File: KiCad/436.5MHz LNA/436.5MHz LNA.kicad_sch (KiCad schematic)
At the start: 15 parts, among them J1 Conn_Coaxial, J2 Conn_Coaxial, J3 +9V, Q1 J310

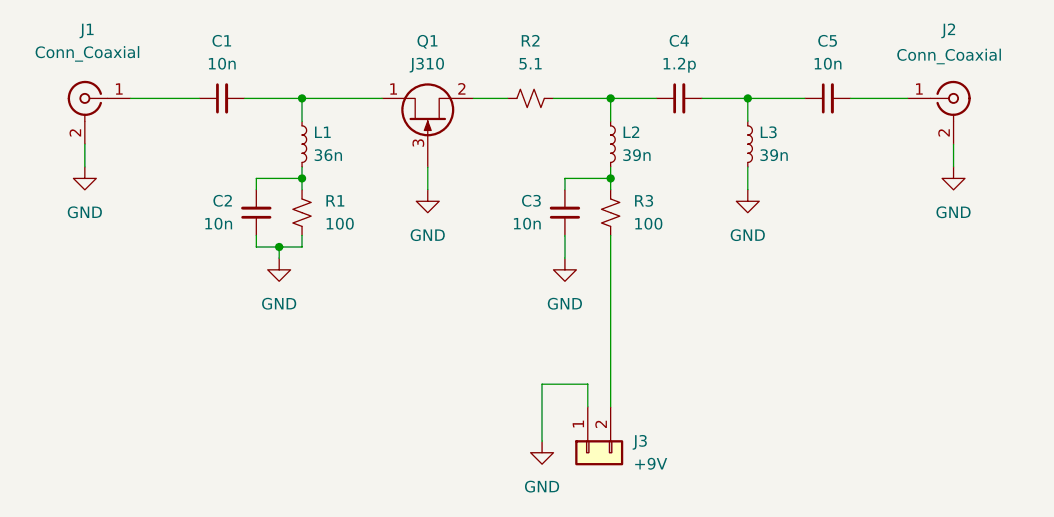
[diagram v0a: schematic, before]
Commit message: added BOM
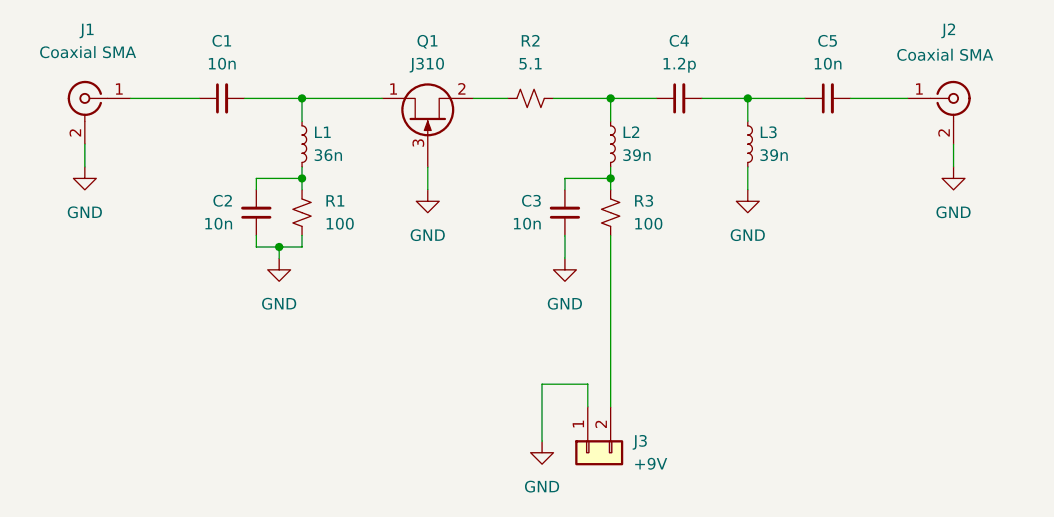
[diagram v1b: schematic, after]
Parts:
- J1, J2: value Conn_Coaxial -> Coaxial SMA
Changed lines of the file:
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@@
   (title_block
     (title "436.5MHz LNA")
+    (rev "1.0")
     (company "KK7DLH")
   )
@@
     (in_bom yes) (on_board yes) (fields_autoplaced)
     (property "Reference" "J1" (id 0) (at 94.2974 81.28 0))
-    (property "Value" "Conn_Coaxial" (id 1) (at 94.2974 83.82 0))
+    (property "Value" "Coaxial SMA" (id 1) (at 94.2974 83.82 0))
     (property "Footprint" "Connector_Coaxial:SMA_Amphenol_132289_EdgeMount" (id 2) (at 93.98 88.9 0)
       (effects (font (size 1.27 1.27)) hide)
@@
       (effects (font (size 1.27 1.27)) (justify left))
     )
-    (property "Value" "Conn_Coaxial" (id 1) (at 184.15 84.1131 0)
+    (property "Value" "Coaxial SMA" (id 1) (at 184.15 84.1131 0)
       (effects (font (size 1.27 1.27)) (justify left))
     )
@@
     )
     (path "/e04409c2-b3ba-460e-bddc-62e0044901c2"
-      (reference "J1") (unit 1) (value "Conn_Coaxial") (footprint "Connector_Coaxial:SMA_Amphenol_132289_EdgeMount")
+      (reference "J1") (unit 1) (value "Coaxial SMA") (footprint "Connector_Coaxial:SMA_Amphenol_132289_EdgeMount")
     )
     (path "/f0ff0792-4d97-4881-9b9c-759645b25c42"
-      (reference "J2") (unit 1) (value "Conn_Coaxial") (footprint "Connector_Coaxial:SMA_Amphenol_132289_EdgeMount")
+      (reference "J2") (unit 1) (value "Coaxial SMA") (footprint "Connector_Coaxial:SMA_Amphenol_132289_EdgeMount")
     )
     (path "/45c0d4b2-152f-4522-afdb-d5657a7cd4e7"

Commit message: updated bom to purchase inductors from coilcraft and to remove most parts with terifs
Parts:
- C1, C2, C3, C5: DPN 478-10055-2-ND -> 1276-1091-2-ND; MFN KYOCERA AVX -> Samsung Electro-Mechanics; MPN 06035C103KAT4A -> CL10C102JB8NNNC
- C4: DPN 311-3825-2-ND -> 311-3825-1-ND‎; MPN CC0603BRNPO9BN1R2 -> CC0603BRNPO9BN1R2‎
- J1, J2: DPN 314-1702-ND -> 314-1702-ND‎
- L1: DPN 2457-0603DC-36NXJRW-ND -> 0603DC-36NXJRW; Dist DigiKey -> Coilcraft
- L2, L3: DPN 2457-0603DC-39NXJRW-ND -> 0603DC-39NXJRW; Dist DigiKey -> Coilcraft
- Q1: DPN MMBFJ310LT3GOSTR-ND -> MMBFJ310LT3GOSCT-ND‎
- R1, R3: DPN 541-CRCW0603100RFKEBCTR-ND -> A129676TR-ND; MFN Vishay Dale -> TE Connectivity Passive Product; MPN CRCW0603100RFKEBC -> CRGCQ0603F100R
- R2: DPN YAG3372TR-ND -> YAG3372CT-ND‎
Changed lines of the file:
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@@
       (effects (font (size 1.27 1.27)) hide)
     )
-    (property "DPN" "478-10055-2-ND" (id 5) (at 109.22 88.9 0)
-      (effects (font (size 1.27 1.27)) hide)
-    )
-    (property "MFN" "KYOCERA AVX" (id 6) (at 109.22 88.9 0)
-      (effects (font (size 1.27 1.27)) hide)
-    )
-    (property "MPN" "06035C103KAT4A" (id 7) (at 109.22 88.9 0)
+    (property "DPN" "1276-1091-2-ND" (id 5) (at 109.22 88.9 0)
+      (effects (font (size 1.27 1.27)) hide)
+    )
+    (property "MFN" "Samsung Electro-Mechanics" (id 6) (at 109.22 88.9 0)
+      (effects (font (size 1.27 1.27)) hide)
+    )
+    (property "MPN" "CL10C102JB8NNNC" (id 7) (at 109.22 88.9 0)
       (effects (font (size 1.27 1.27)) hide)
     )
@@
       (effects (font (size 1.27 1.27)) hide)
     )
-    (property "DPN" "541-CRCW0603100RFKEBCTR-ND" (id 5) (at 118.11 101.6 0)
-      (effects (font (size 1.27 1.27)) hide)
-    )
-    (property "MFN" "Vishay Dale" (id 6) (at 118.11 101.6 0)
-      (effects (font (size 1.27 1.27)) hide)
-    )
-    (property "MPN" "CRCW0603100RFKEBC" (id 7) (at 118.11 101.6 0)
+    (property "DPN" "A129676TR-ND" (id 5) (at 118.11 101.6 0)
+      (effects (font (size 1.27 1.27)) hide)
+    )
+    (property "MFN" "TE Connectivity Passive Product" (id 6) (at 118.11 101.6 0)
+      (effects (font (size 1.27 1.27)) hide)
+    )
+    (property "MPN" "CRGCQ0603F100R" (id 7) (at 118.11 101.6 0)
       (effects (font (size 1.27 1.27)) hide)
     )
@@
       (effects (font (size 1.27 1.27)) hide)
     )
-    (property "Dist" "DigiKey" (id 6) (at 167.64 93.98 0)
-      (effects (font (size 1.27 1.27)) hide)
-    )
-    (property "DPN" "2457-0603DC-39NXJRW-ND" (id 7) (at 167.64 93.98 0)
+    (property "Dist" "Coilcraft" (id 6) (at 167.64 93.98 0)
+      (effects (font (size 1.27 1.27)) hide)
+    )
+    (property "DPN" "0603DC-39NXJRW" (id 7) (at 167.64 93.98 0)
       (effects (font (size 1.27 1.27)) hide)
     )
@@
       (effects (font (size 1.27 1.27)) hide)
     )
-    (property "DPN" "2457-0603DC-36NXJRW-ND" (id 4) (at 118.11 93.98 0)
-      (effects (font (size 1.27 1.27)) hide)
-    )
-    (property "Dist" "DigiKey" (id 5) (at 118.11 93.98 0)
+    (property "DPN" "0603DC-36NXJRW" (id 4) (at 118.11 93.98 0)
+      (effects (font (size 1.27 1.27)) hide)
+    )
+    (property "Dist" "Coilcraft" (id 5) (at 118.11 93.98 0)
       (effects (font (size 1.27 1.27)) hide)
     )
@@
       (effects (font (size 1.27 1.27)) hide)
     )
-    (property "DPN" "478-10055-2-ND" (id 5) (at 176.53 88.9 0)
-      (effects (font (size 1.27 1.27)) hide)
-    )
-    (property "MFN" "KYOCERA AVX" (id 6) (at 176.53 88.9 0)
-      (effects (font (size 1.27 1.27)) hide)
-    )
-    (property "MPN" "06035C103KAT4A" (id 7) (at 176.53 88.9 0)
+    (property "DPN" "1276-1091-2-ND" (id 5) (at 176.53 88.9 0)
+      (effects (font (size 1.27 1.27)) hide)
+    )
+    (property "MFN" "Samsung Electro-Mechanics" (id 6) (at 176.53 88.9 0)
+      (effects (font (size 1.27 1.27)) hide)
+    )
+    (property "MPN" "CL10C102JB8NNNC" (id 7) (at 176.53 88.9 0)
       (effects (font (size 1.27 1.27)) hide)
     )
@@
       (effects (font (size 1.27 1.27)) hide)
     )
-    (property "DPN" "541-CRCW0603100RFKEBCTR-ND" (id 5) (at 152.4 101.6 0)
-      (effects (font (size 1.27 1.27)) hide)
-    )
-    (property "MFN" "Vishay Dale" (id 6) (at 152.4 101.6 0)
-      (effects (font (size 1.27 1.27)) hide)
-    )
-    (property "MPN" "CRCW0603100RFKEBC" (id 7) (at 152.4 101.6 0)
+    (property "DPN" "A129676TR-ND" (id 5) (at 152.4 101.6 0)
+      (effects (font (size 1.27 1.27)) hide)
+    )
+    (property "MFN" "TE Connectivity Passive Product" (id 6) (at 152.4 101.6 0)
+      (effects (font (size 1.27 1.27)) hide)
+    )
+    (property "MPN" "CRGCQ0603F100R" (id 7) (at 152.4 101.6 0)
       (effects (font (size 1.27 1.27)) hide)
     )
@@
       (effects (font (size 1.27 1.27)) hide)
     )
-    (property "DPN" "478-10055-2-ND" (id 5) (at 147.32 101.6 0)
-      (effects (font (size 1.27 1.27)) hide)
-    )
-    (property "MFN" "KYOCERA AVX" (id 6) (at 147.32 101.6 0)
-      (effects (font (size 1.27 1.27)) hide)
-    )
-    (property "MPN" "06035C103KAT4A" (id 7) (at 147.32 101.6 0)
+    (property "DPN" "1276-1091-2-ND" (id 5) (at 147.32 101.6 0)
+      (effects (font (size 1.27 1.27)) hide)
+    )
+    (property "MFN" "Samsung Electro-Mechanics" (id 6) (at 147.32 101.6 0)
+      (effects (font (size 1.27 1.27)) hide)
+    )
+    (property "MPN" "CL10C102JB8NNNC" (id 7) (at 147.32 101.6 0)
       (effects (font (size 1.27 1.27)) hide)
     )
@@
       (effects (font (size 1.27 1.27)) hide)
     )
-    (property "DPN" "311-3825-2-ND" (id 5) (at 160.02 88.9 0)
+    (property "DPN" "311-3825-1-ND‎" (id 5) (at 160.02 88.9 0)
       (effects (font (size 1.27 1.27)) hide)
     )
@@
       (effects (font (size 1.27 1.27)) hide)
     )
-    (property "MPN" "CC0603BRNPO9BN1R2" (id 7) (at 160.02 88.9 0)
+    (property "MPN" "CC0603BRNPO9BN1R2‎ " (id 7) (at 160.02 88.9 0)
       (effects (font (size 1.27 1.27)) hide)
     )
@@
       (effects (font (size 1.27 1.27)) hide)
     )
-    (property "DPN" "314-1702-ND" (id 5) (at 93.98 88.9 0)
+    (property "DPN" "314-1702-ND‎" (id 5) (at 93.98 88.9 0)
       (effects (font (size 1.27 1.27)) hide)
     )
@@
       (effects (font (size 1.27 1.27)) hide)
     )
-    (property "DPN" "YAG3372TR-ND" (id 5) (at 143.51 88.9 0)
+    (property "DPN" "YAG3372CT-ND‎" (id 5) (at 143.51 88.9 0)
       (effects (font (size 1.27 1.27)) hide)
     )
@@
       (effects (font (size 1.27 1.27)) hide)
     )
-    (property "DPN" "478-10055-2-ND" (id 5) (at 113.03 101.6 0)
-      (effects (font (size 1.27 1.27)) hide)
-    )
-    (property "MFN" "KYOCERA AVX" (id 6) (at 113.03 101.6 0)
-      (effects (font (size 1.27 1.27)) hide)
-    )
-    (property "MPN" "06035C103KAT4A" (id 7) (at 113.03 101.6 0)
+    (property "DPN" "1276-1091-2-ND" (id 5) (at 113.03 101.6 0)
+      (effects (font (size 1.27 1.27)) hide)
+    )
+    (property "MFN" "Samsung Electro-Mechanics" (id 6) (at 113.03 101.6 0)
+      (effects (font (size 1.27 1.27)) hide)
+    )
+    (property "MPN" "CL10C102JB8NNNC" (id 7) (at 113.03 101.6 0)
       (effects (font (size 1.27 1.27)) hide)
     )
@@
       (effects (font (size 1.27 1.27)) hide)
     )
-    (property "DPN" "MMBFJ310LT3GOSTR-ND" (id 4) (at 132.08 91.44 0)
+    (property "DPN" "MMBFJ310LT3GOSCT-ND‎" (id 4) (at 132.08 91.44 0)
       (effects (font (size 1.27 1.27)) hide)
     )
@@
       (effects (font (size 1.27 1.27)) hide)
     )
-    (property "DPN" "314-1702-ND" (id 5) (at 190.5 88.9 0)
+    (property "DPN" "314-1702-ND‎" (id 5) (at 190.5 88.9 0)
       (effects (font (size 1.27 1.27)) hide)
     )
@@
       (effects (font (size 1.27 1.27)) hide)
     )
-    (property "DPN" "2457-0603DC-39NXJRW-ND" (id 4) (at 152.4 93.98 0)
-      (effects (font (size 1.27 1.27)) hide)
-    )
-    (property "Dist" "DigiKey" (id 5) (at 152.4 93.98 0)
-      (effects (font (size 1.27 1.27)) hide)
-    )
+    (property "DPN" "0603DC-39NXJRW" (id 4) (at 152.4 93.98 0)
+      (effects (font (size 1.27 1.27)) hide)
+    )
+    (property "Dist" "Coilcraft" (id 5) (at 152.4 93.98 0)
+      (effects (font (size 1.27 1.27)) hide)
+    )

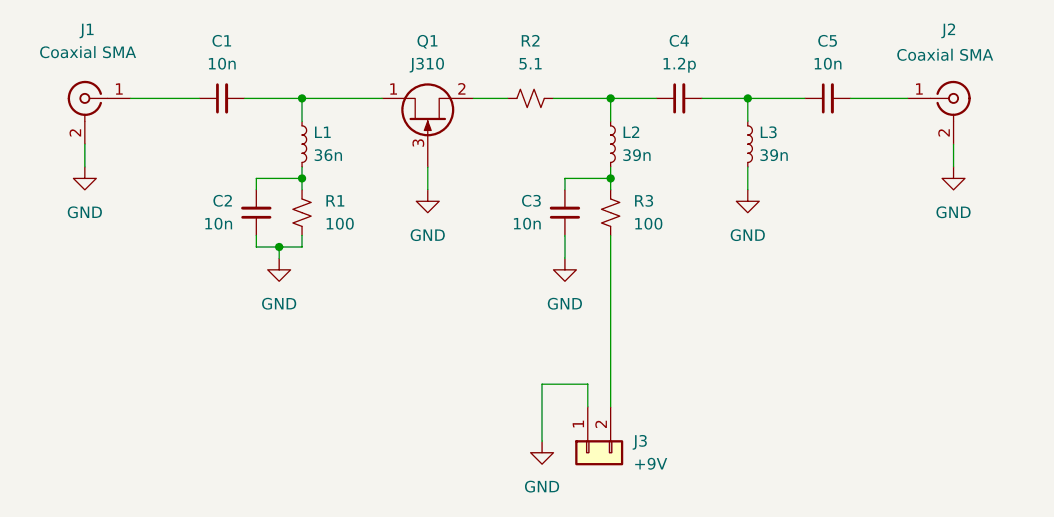
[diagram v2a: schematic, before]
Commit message: flipped the JFET so the gate has a more common ground with the RF path
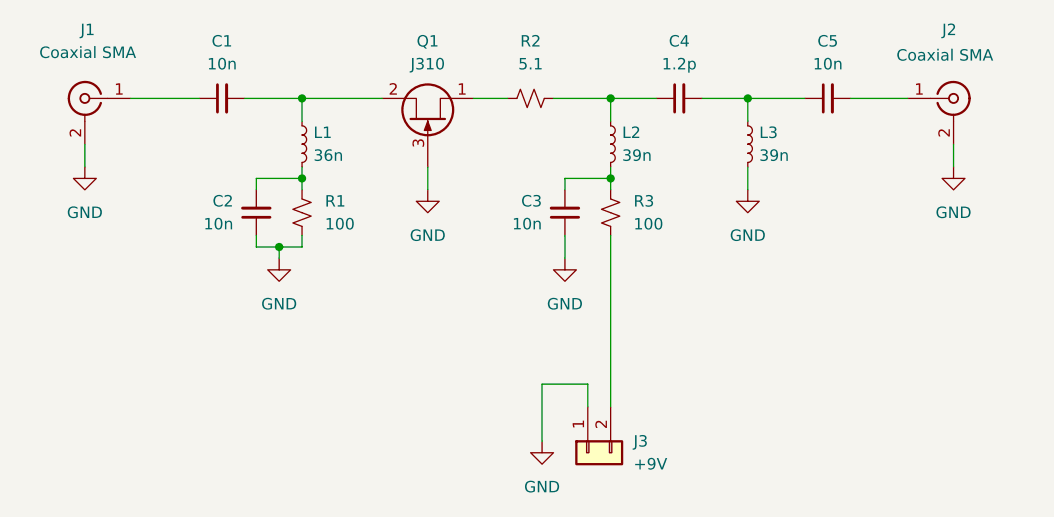
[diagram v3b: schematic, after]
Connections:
- net at C1.2, L1.1: now also Q1.2 (S); no longer Q1.1 (D)
- net at R2.1: now also Q1.1 (D); no longer Q1.2 (S)
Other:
- moved on the sheet: Q1
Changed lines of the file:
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@@
     (pin "2")
   )
-  (symbol (lib_id "Device:Q_NJFET_DSG") (at 132.08 91.44 90) (unit 1)
+  (symbol (lib_id "Device:Q_NJFET_DSG") (at 132.08 91.44 270) (mirror x) (unit 1)
     (in_bom yes) (on_board yes) (fields_autoplaced)
     (property "Reference" "Q1" (id 0) (at 132.08 82.55 90))
     (property "Value" "J310" (id 1) (at 132.08 85.09 90))
-    (property "Footprint" "Package_TO_SOT_SMD:SOT-23" (id 2) (at 129.54 86.36 0)
+    (property "Footprint" "Package_TO_SOT_SMD:SOT-23" (id 2) (at 134.62 86.36 0)
       (effects (font (size 1.27 1.27)) hide)
     )
